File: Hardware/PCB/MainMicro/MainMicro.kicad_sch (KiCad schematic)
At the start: 13 parts

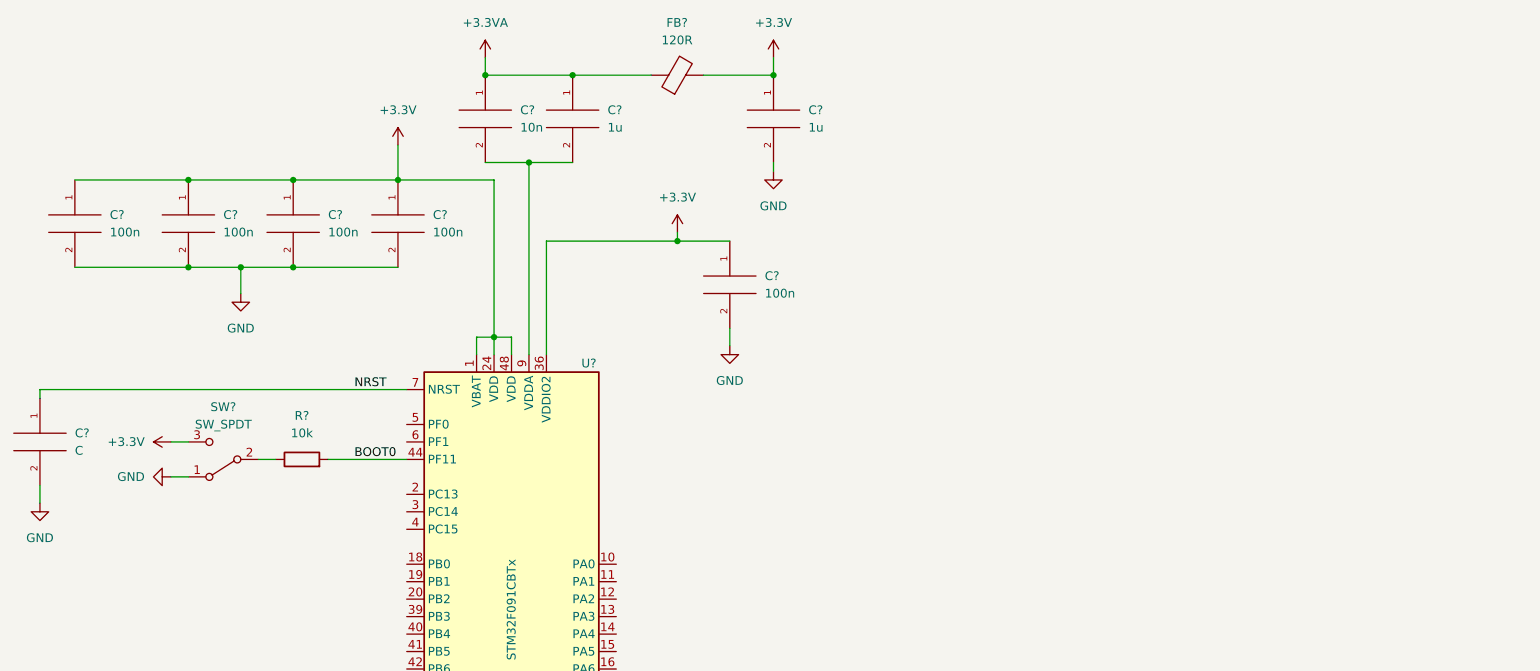
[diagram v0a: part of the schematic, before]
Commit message: Started USB 2.0 Support Interface
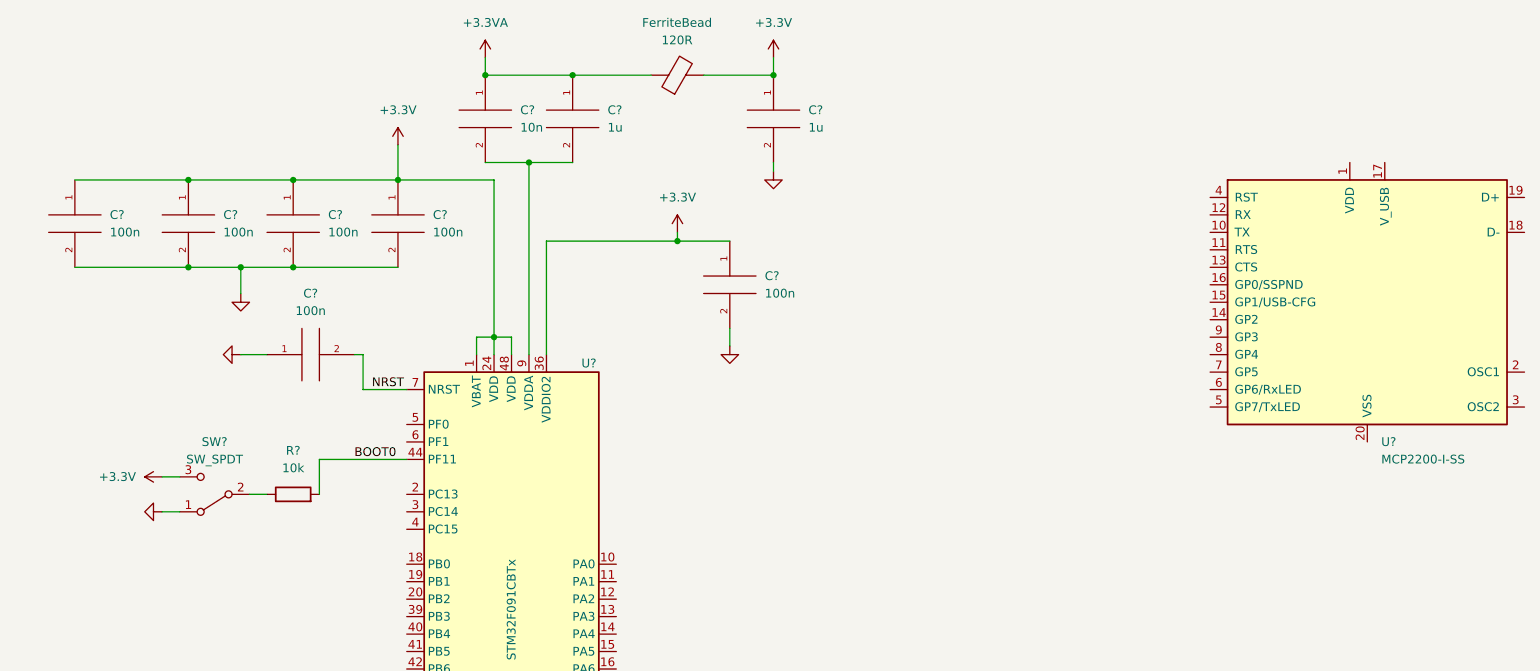
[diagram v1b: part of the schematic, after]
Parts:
- added U?: MCP2200-I-SS, Package_SO:SSOP-20_5.3x7.2mm_P0.65mm, symbol Interface_USB:MCP2200-I-SS
- C?: value C -> 100n
- gave numbers to parts that had none: 1
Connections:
- net GND: now also C?.1; no longer C?.2
- net NRST: now also C?.2; no longer C?.1
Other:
- moved on the sheet: C?, R?, SW?

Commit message: Small cleanup to sch
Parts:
- added J?: USB_B_Mini, symbol Connector:USB_B_Mini
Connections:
- net GND: now also U?.20 (VSS), J?.5 (GND)
- net at U?.10 (PA0): now also U?.13 (CTS)
- net at U?.11 (PA1): now also U?.11 (RTS)
- net at U?.12 (PA2): now also U?.10 (TX)
- net at U?.13 (PA3): now also U?.12 (RX)
- net at U?.17 (V_USB): now also J?.1 (VBUS)
- net at U?.18 (D-): now also J?.2 (D-)
- net at U?.19 (D+): now also J?.3 (D+)
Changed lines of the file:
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@@
+    (stroke (width 0) (type default) (color 0 0 0 0))
+  )
+  (wire (pts (xy 166.37 110.49) (xy 166.37 52.07))
     (stroke (width 0) (type default) (color 0 0 0 0))
   )
@@
     (stroke (width 0) (type default) (color 0 0 0 0))
   )
+  (wire (pts (xy 161.29 57.15) (xy 186.69 57.15))
+    (stroke (width 0) (type default) (color 0 0 0 0))
+  )
+  (wire (pts (xy 247.65 39.37) (xy 212.09 39.37))
+    (stroke (width 0) (type default) (color 0 0 0 0))
+  )
+  (wire (pts (xy 251.46 53.34) (xy 237.49 53.34))
+    (stroke (width 0) (type default) (color 0 0 0 0))
+  )
+  (wire (pts (xy 163.83 107.95) (xy 163.83 54.61))
+    (stroke (width 0) (type default) (color 0 0 0 0))
+  )
   (wire (pts (xy 109.22 55.88) (xy 90.17 55.88))
     (stroke (width 0) (type default) (color 0 0 0 0))
@@
     (stroke (width 0) (type default) (color 0 0 0 0))
   )
+  (wire (pts (xy 100.33 105.41) (xy 161.29 105.41))
+    (stroke (width 0) (type default) (color 0 0 0 0))
+  )
   (wire (pts (xy 80.01 148.59) (xy 80.01 149.86))
     (stroke (width 0) (type default) (color 0 0 0 0))
@@
     (stroke (width 0) (type default) (color 0 0 0 0))
   )
+  (wire (pts (xy 237.49 54.61) (xy 232.41 54.61))
+    (stroke (width 0) (type default) (color 0 0 0 0))
+  )
   (wire (pts (xy 90.17 55.88) (xy 90.17 72.39))
     (stroke (width 0) (type default) (color 0 0 0 0))
@@
     (stroke (width 0) (type default) (color 0 0 0 0))
   )
+  (wire (pts (xy 158.75 102.87) (xy 158.75 59.69))
+    (stroke (width 0) (type default) (color 0 0 0 0))
+  )
+  (wire (pts (xy 100.33 107.95) (xy 163.83 107.95))
+    (stroke (width 0) (type default) (color 0 0 0 0))
+  )
   (wire (pts (xy 87.63 44.45) (xy 87.63 72.39))
     (stroke (width 0) (type default) (color 0 0 0 0))
@@
     (stroke (width 0) (type default) (color 0 0 0 0))
   )
+  (wire (pts (xy 237.49 49.53) (xy 237.49 50.8))
+    (stroke (width 0) (type default) (color 0 0 0 0))
+  )
+  (wire (pts (xy 259.08 63.5) (xy 259.08 60.96))
+    (stroke (width 0) (type default) (color 0 0 0 0))
+  )
   (wire (pts (xy 57.15 87.63) (xy 69.85 87.63))
     (stroke (width 0) (type default) (color 0 0 0 0))
@@
     (stroke (width 0) (type default) (color 0 0 0 0))
   )
+  (wire (pts (xy 237.49 50.8) (xy 251.46 50.8))
+    (stroke (width 0) (type default) (color 0 0 0 0))
+  )
   (wire (pts (xy 82.55 148.59) (xy 80.01 148.59))
     (stroke (width 0) (type default) (color 0 0 0 0))
   )
+  (wire (pts (xy 161.29 105.41) (xy 161.29 57.15))
+    (stroke (width 0) (type default) (color 0 0 0 0))
+  )
   (wire (pts (xy 85.09 69.85) (xy 82.55 69.85))
     (stroke (width 0) (type default) (color 0 0 0 0))
@@
     (stroke (width 0) (type default) (color 0 0 0 0))
   )
+  (wire (pts (xy 232.41 49.53) (xy 237.49 49.53))
+    (stroke (width 0) (type default) (color 0 0 0 0))
+  )
+  (wire (pts (xy 100.33 110.49) (xy 166.37 110.49))
+    (stroke (width 0) (type default) (color 0 0 0 0))
+  )
   (wire (pts (xy 87.63 44.45) (xy 93.98 44.45))
     (stroke (width 0) (type default) (color 0 0 0 0))
@@
     (stroke (width 0) (type default) (color 0 0 0 0))
   )
+  (wire (pts (xy 163.83 54.61) (xy 186.69 54.61))
+    (stroke (width 0) (type default) (color 0 0 0 0))
+  )
+  (wire (pts (xy 166.37 52.07) (xy 186.69 52.07))
+    (stroke (width 0) (type default) (color 0 0 0 0))
+  )
   (wire (pts (xy 63.5 77.47) (xy 69.85 77.47))
     (stroke (width 0) (type default) (color 0 0 0 0))
   )
+  (wire (pts (xy 247.65 45.72) (xy 247.65 39.37))
+    (stroke (width 0) (type default) (color 0 0 0 0))
+  )
   (wire (pts (xy 82.55 46.99) (xy 82.55 69.85))
     (stroke (width 0) (type default) (color 0 0 0 0))
@@
     (stroke (width 0) (type default) (color 0 0 0 0))
   )
+  (wire (pts (xy 158.75 59.69) (xy 186.69 59.69))
+    (stroke (width 0) (type default) (color 0 0 0 0))
+  )
+  (wire (pts (xy 100.33 102.87) (xy 158.75 102.87))
+    (stroke (width 0) (type default) (color 0 0 0 0))
+  )
   (wire (pts (xy 93.98 31.75) (xy 105.41 31.75))
     (stroke (width 0) (type default) (color 0 0 0 0))
@@
     (stroke (width 0) (type default) (color 0 0 0 0))
   )
+  (wire (pts (xy 212.09 39.37) (xy 212.09 44.45))
+    (stroke (width 0) (type default) (color 0 0 0 0))
+  )
   (wire (pts (xy 109.22 54.61) (xy 109.22 55.88))
     (stroke (width 0) (type default) (color 0 0 0 0))
@@
     (stroke (width 0) (type default) (color 0 0 0 0))
   )
+  (wire (pts (xy 237.49 53.34) (xy 237.49 54.61))
+    (stroke (width 0) (type default) (color 0 0 0 0))
+  )
+  (wire (pts (xy 209.55 85.09) (xy 209.55 90.17))
+    (stroke (width 0) (type default) (color 0 0 0 0))
+  )
   (wire (pts (xy 82.55 146.05) (xy 82.55 148.59))
+    (stroke (width 0) (type default) (color 0 0 0 0))
+  )
+  (wire (pts (xy 251.46 45.72) (xy 247.65 45.72))
     (stroke (width 0) (type default) (color 0 0 0 0))
   )
@@
     (pin "1")
     (pin "2")
+  )
+  (symbol (lib_id "power:GND") (at 209.55 90.17 0) (unit 1)
+    (in_bom yes) (on_board yes) (fields_autoplaced)
+    (property "Reference" "#PWR?" (id 0) (at 209.55 96.52 0)
+      (effects (font (size 1.27 1.27)) hide)
+    )
+    (property "Value" "GND" (id 1) (at 209.55 95.25 0)
+      (effects (font (size 1.27 1.27)) hide)
+    )
+    (property "Footprint" "" (id 2) (at 209.55 90.17 0)
+      (effects (font (size 1.27 1.27)) hide)
+    )
+    (property "Datasheet" "" (id 3) (at 209.55 90.17 0)
+      (effects (font (size 1.27 1.27)) hide)
+    )
+    (pin "1")
   )
   (symbol (lib_id "power:+3.3V") (at 123.19 29.21 0) (unit 1)
@@
     (pin "9")
   )
+  (symbol (lib_id "Connector:USB_B_Mini") (at 259.08 50.8 0) (mirror y) (unit 1)
+    (in_bom yes) (on_board yes) (fields_autoplaced)
+    (property "Reference" "J?" (id 0) (at 265.43 49.5299 0)
+      (effects (font (size 1.27 1.27)) (justify right))
+    )
+    (property "Value" "USB_B_Mini" (id 1) (at 265.43 52.0699 0)
+      (effects (font (size 1.27 1.27)) (justify right))
+    )
+    (property "Footprint" "" (id 2) (at 255.27 52.07 0)
+      (effects (font (size 1.27 1.27)) hide)
+    )
+    (property "Datasheet" "~" (id 3) (at 255.27 52.07 0)
+      (effects (font (size 1.27 1.27)) hide)
+    )
+    (pin "1")
+    (pin "2")
+    (pin "3")
+    (pin "4")
+    (pin "5")
+    (pin "6")
+  )
   (symbol (lib_id "pspice:C") (at 123.19 38.1 0) (unit 1)
     (in_bom yes) (on_board yes) (fields_autoplaced)
@@
     (pin "3")
   )
+  (symbol (lib_id "power:GND") (at 259.08 63.5 0) (unit 1)
+    (in_bom yes) (on_board yes) (fields_autoplaced)
+    (property "Reference" "#PWR?" (id 0) (at 259.08 69.85 0)
+      (effects (font (size 1.27 1.27)) hide)
+    )
+    (property "Value" "GND" (id 1) (at 259.08 68.58 0)
+      (effects (font (size 1.27 1.27)) hide)
+    )
+    (property "Footprint" "" (id 2) (at 259.08 63.5 0)
+      (effects (font (size 1.27 1.27)) hide)
+    )
+    (property "Datasheet" "" (id 3) (at 259.08 63.5 0)
+      (effects (font (size 1.27 1.27)) hide)
+    )
+    (pin "1")
+  )
   (symbol (lib_id "power:GND") (at 34.29 95.25 270) (unit 1)
     (in_bom yes) (on_board yes) (fields_autoplaced)
@@
       (reference "#PWR?") (unit 1) (value "+3.3V") (footprint "")
     )
+    (path "/19dac2f1-7ff1-458f-a046-1f6b9bcbe5bf"
+      (reference "#PWR?") (unit 1) (value "GND") (footprint "")
+    )
     (path "/3a905bbd-e2e6-4aab-89db-ca02168627ab"
       (reference "#PWR?") (unit 1) (value "+3.3V") (footprint "")
@@
       (reference "#PWR?") (unit 1) (value "+3.3V") (footprint "")
     )
+    (path "/a60131c7-786e-4b04-98f8-e59653010a0e"
+      (reference "#PWR?") (unit 1) (value "GND") (footprint "")
+    )
     (path "/b334c0de-39bf-4fe1-9b7f-3e68a088d6de"
       (reference "#PWR?") (unit 1) (value "GND") (footprint "")
@@
       (reference "FerriteBead") (unit 1) (value "120R") (footprint "")
     )
+    (path "/873c612d-f5e5-451f-9631-74bf26e685d0"
+      (reference "J?") (unit 1) (value "USB_B_Mini") (footprint "")
+    )
     (path "/5196bea8-c995-4c03-a88a-582c13c03f8c"

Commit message: More PCB stuff
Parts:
- removed U?: MCP2200-I-SS, Package_SO:SSOP-20_5.3x7.2mm_P0.65mm, symbol Interface_USB:MCP2200-I-SS
- added C? (x2): 100n, symbol pspice:C
- added J?: Conn_ARM_JTAG_SWD_10, symbol Connector:Conn_ARM_JTAG_SWD_10
- added U? (x2): 74HC595, symbol 74xx:74HC595
- added U?: FT232RL, Package_SO:SSOP-28_5.3x10.2mm_P0.65mm, symbol Interface_USB:FT232RL
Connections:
- net +3V3: now also J?.1 (VBUS), C?.1, C?.1, U?.19 (~{RESET}), U?.20 (VCC), U?.4 (VCCIO)
- net GND: now also C?.2, C?.2, U?.13 (~{OE}), U?.13 (~{OE}), U?.18 (GND), U?.21 (GND), U?.25 (AGND), U?.26 (TEST), U?.7 (GND), U?.8 (GND), U?.8 (GND)
- net CTS: now reaches U?.10 (PA0)
- net CTS: now also U?.11 (CTS)
- net RTS: now reaches U?.11 (PA1)
- net RTS: now also U?.3 (RTS)
- net TX: now reaches U?.12 (PA2)
- net TX: now also U?.1 (TXD)
- net RX: now reaches U?.13 (PA3)
- net RX: now also U?.5 (RXD)
- net at U?.15 (PA5): now also U?.11 (SRCLK), U?.11 (SRCLK)
- net at U?.16 (PA6): now also U?.12 (RCLK), U?.12 (RCLK)
- net at U?.17 (PA7): now also J?.3 (GND), J?.5 (GND), J?.9 (GNDDetect), U?.14 (SER)
- net at U?.34 (PA13): now also J?.2 (SWDIO/TMS)
- net at U?.37 (PA14): now also J?.4 (SWDCLK/TCK)
- net at J?.2 (D-): now also U?.16 (USBD-)
- net at J?.3 (D+): now also U?.15 (USBD+)
- new net: U?.14 (SER), U?.9 (QH')
- new net To 8 Pin display selector: U?.3 (QD)
- new net To 8 pin segment selector: U?.4 (QE)
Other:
- moved on the sheet: J?

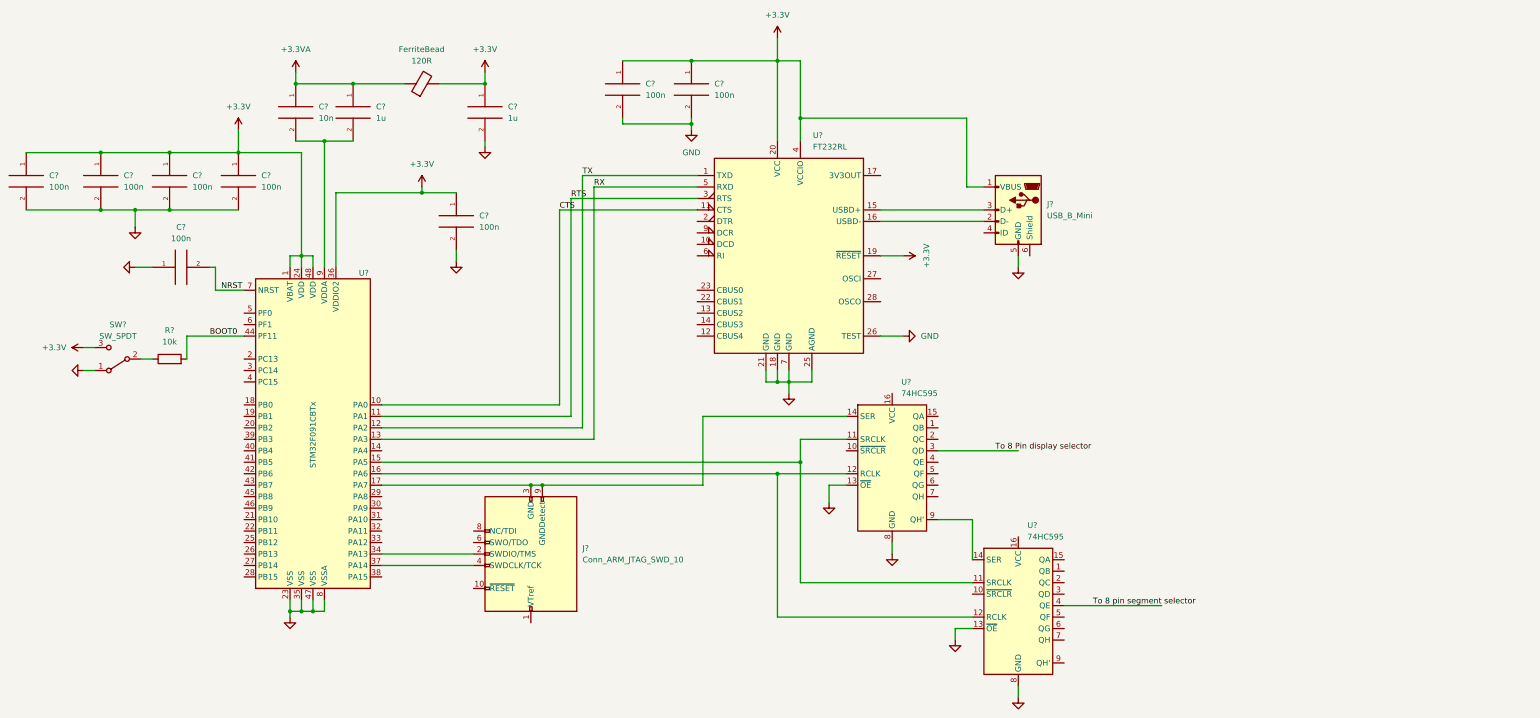
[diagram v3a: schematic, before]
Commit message: PCB Power Supply + General Changes
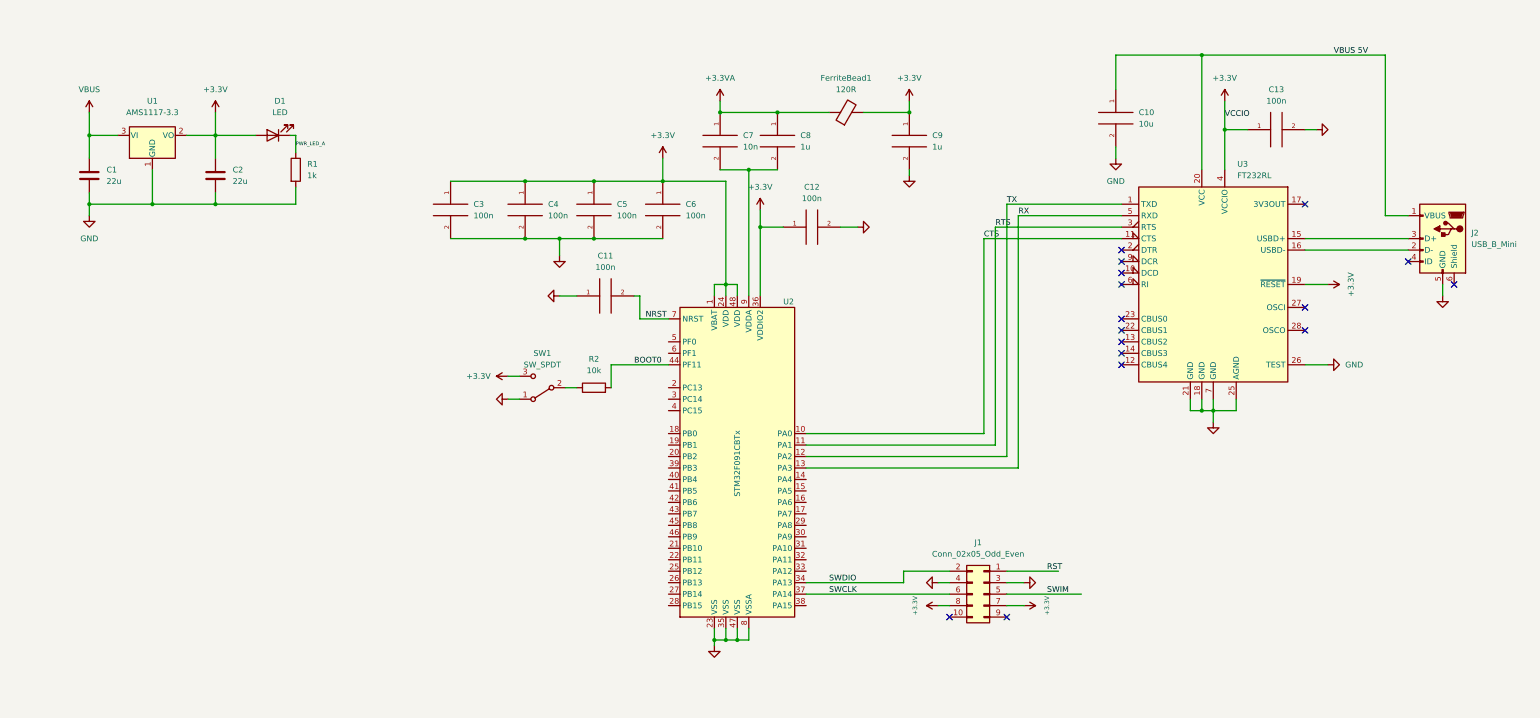
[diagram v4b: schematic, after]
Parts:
- removed C?: 100n, symbol pspice:C
- removed J?: Conn_ARM_JTAG_SWD_10, symbol Connector:Conn_ARM_JTAG_SWD_10
- removed U? (x2): 74HC595, symbol 74xx:74HC595
- added C1, C2: 22u, Capacitor_SMD:C_0805_2012Metric_Pad1.18x1.45mm_HandSolder, symbol Device:C
- added C13: 100n, Capacitor_SMD:C_0805_2012Metric_Pad1.18x1.45mm_HandSolder, symbol pspice:C
- added D1: LED, LED_SMD:LED_0603_1608Metric_Pad1.05x0.95mm_HandSolder, symbol Device:LED
- added J1: Conn_02x05_Odd_Even, symbol Connector_Generic:Conn_02x05_Odd_Even
- added R1: 1k, Resistor_SMD:R_0805_2012Metric_Pad1.20x1.40mm_HandSolder, symbol Device:R
- added U1: AMS1117-3.3, Package_TO_SOT_SMD:SOT-223-3_TabPin2, symbol Regulator_Linear:AMS1117-3.3
- C10: renamed from C?; value 100n -> 10u; footprint (none) -> Capacitor_SMD:C_0805_2012Metric_Pad1.18x1.45mm_HandSolder
- C11, C12, C3, C4, C5, C6, C7, C8, C9: renamed from C?; footprint (none) -> Capacitor_SMD:C_0805_2012Metric_Pad1.18x1.45mm_HandSolder
- FerriteBead1: renamed from FerriteBead; footprint (none) -> Inductor_SMD:L_0603_1608Metric_Pad1.05x0.95mm_HandSolder
- J2: renamed from J?; footprint (none) -> Connector_USB:USB_Micro-AB_Molex_47590-0001
- R2: renamed from R?; footprint (none) -> Resistor_SMD:R_0805_2012Metric_Pad1.20x1.40mm_HandSolder
- gave numbers to parts that had none: 3
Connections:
- net +3V3: now also C13.1, C2.1, D1.2 (A), J1.7 (Pin_7), J1.8 (Pin_8), U1.2 (VO); no longer C10.1, J2.1 (VBUS), U3.20 (VCC)
- net GND: now also C1.2, C13.2, C2.2, J1.3 (Pin_3), J1.4 (Pin_4), R1.2, U1.1 (GND)
- net SWDIO: now reaches U2.34 (PA13)
- net SWDIO: now also J1.2 (Pin_2)
- net SWCLK: now reaches U2.37 (PA14)
- net SWCLK: now also J1.6 (Pin_6)
- new net PWR_LED_A: D1.1 (K), R1.1
- new net RST: J1.1 (Pin_1)
- new net SWIM: J1.5 (Pin_5)
- new net VBUS: C1.1, U1.3 (VI)
- new net VBUS 5V: C10.1, J2.1 (VBUS), U3.20 (VCC)
- no-connect marks 0 -> 16
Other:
- moved on the sheet: C10, C11, C12, C3, C4, C5, C6, C7, C8, C9, FerriteBead1, J2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

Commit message: PCB workings
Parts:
- removed C11: 100n, Capacitor_SMD:C_0805_2012Metric_Pad1.18x1.45mm_HandSolder, symbol pspice:C
- removed R2: 10k, Resistor_SMD:R_0805_2012Metric_Pad1.20x1.40mm_HandSolder, symbol Device:R
- removed SW1: SW_SPDT, symbol Switch:SW_SPDT
- added C?: C, symbol Device:C
- added D?: LED, symbol Device:LED
- added D?: BAT60JFILM, Diode_SMD:D_SOD-323, symbol Diode:BAT60A
- added J?: Barrel_Jack, symbol Connector:Barrel_Jack
- added R?: 100K, Resistor_SMD:R_0805_2012Metric_Pad1.15x1.40mm_HandSolder, symbol Device:R_US
- added R?: R, symbol Device:R
- added R?: 100k, symbol Device:R
- added SW?: SW_Push, symbol Switch:SW_Push
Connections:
- net +3V3: now also R?.1; no longer J1.8 (Pin_8)
- net BOOT0: now also R?.1
- net GND: now also C?.2, D?.1 (K), J?.2, R?.2, SW?.1
- net NRST: now also C?.1, R?.2, SW?.2
- net SWCLK renamed SWCLK_IN
- net SWDIO renamed SWDIO_IN
- net VBUS renamed +5V
- net +5V: now also D?.1 (K), R?.1
- net VBUS 5V renamed VUSB 5V
- new net: D?.2 (A), R?.2
- new net: D?.2 (A), J?.1
- no-connect marks 16 -> 17
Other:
- moved on the sheet: C1, C10, C13, C2, D1, J1, J2, R1, U1, U3
